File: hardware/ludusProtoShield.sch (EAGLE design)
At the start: 54 parts, among them U1 ARDUINO, U3 TB6612FNG

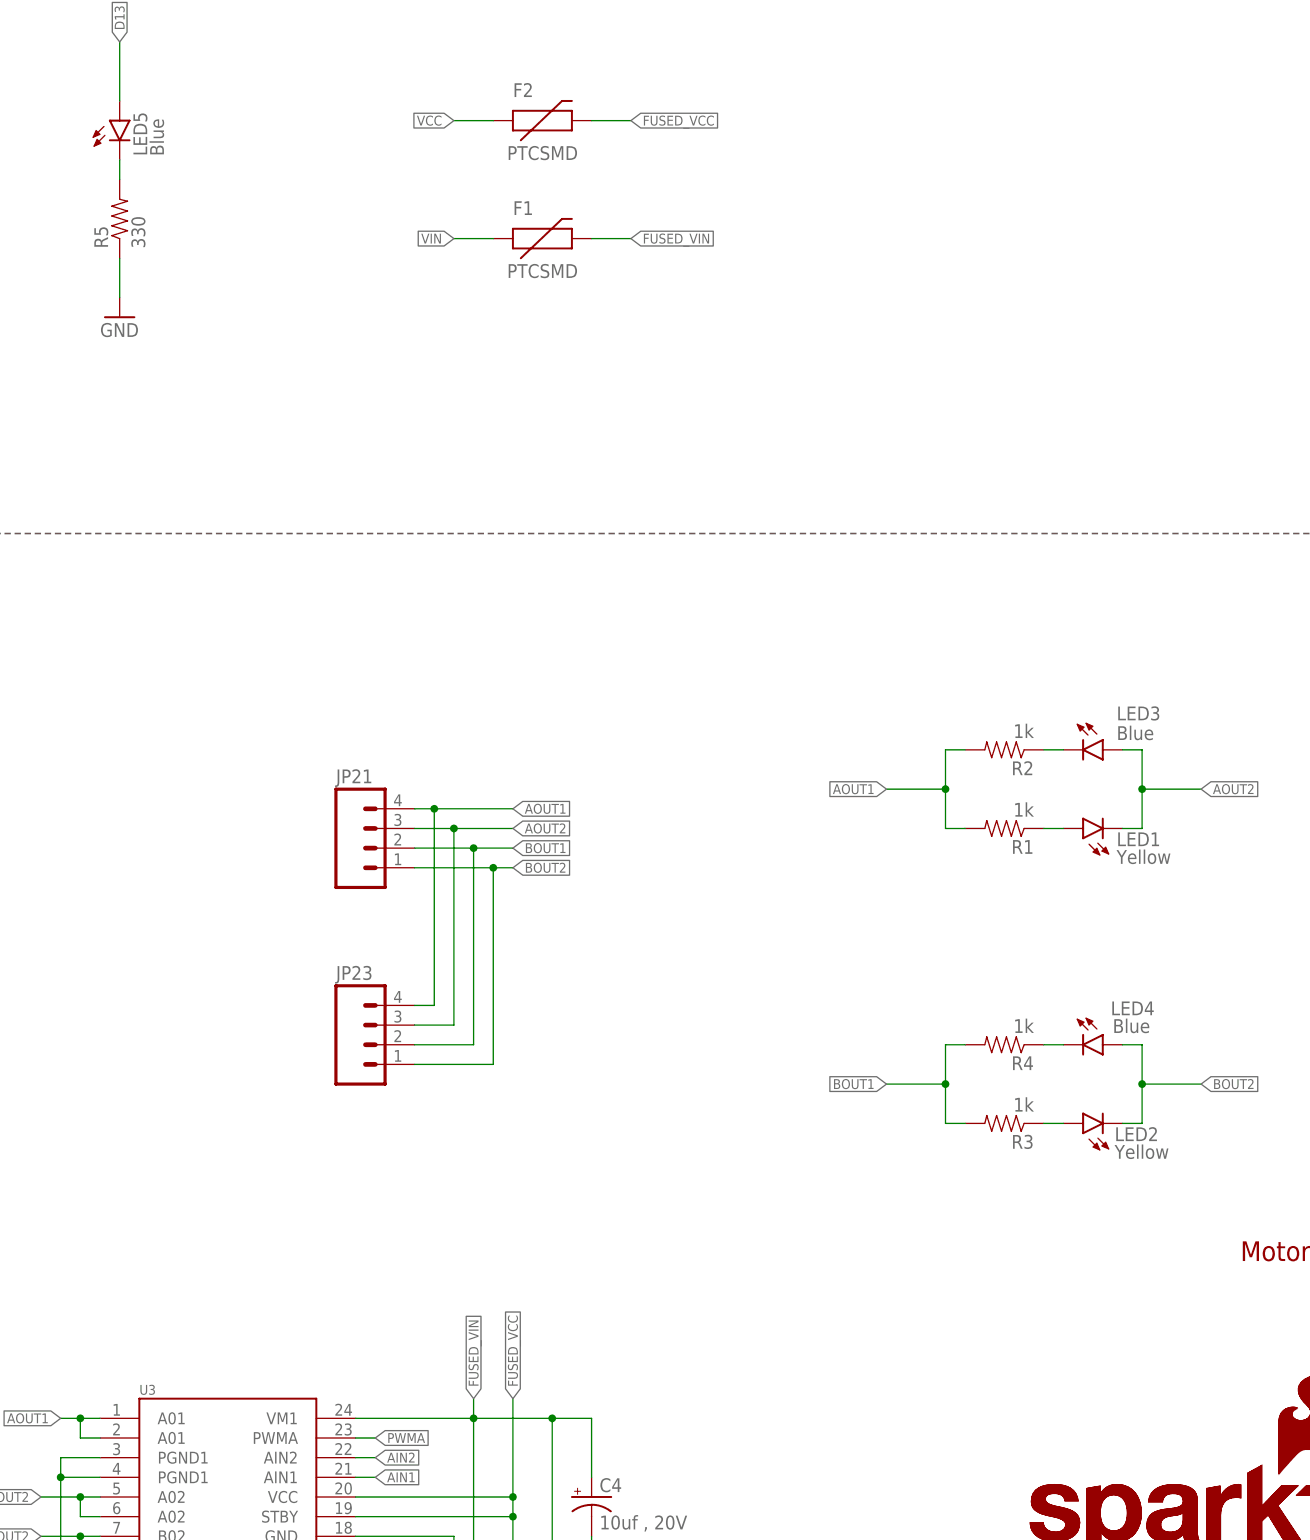
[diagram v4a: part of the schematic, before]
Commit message: Updated libraries and fixed issues from QC for Reds
Updated all of the product libraries and cleaned up extra labels in
hidden layers per issues #10-14
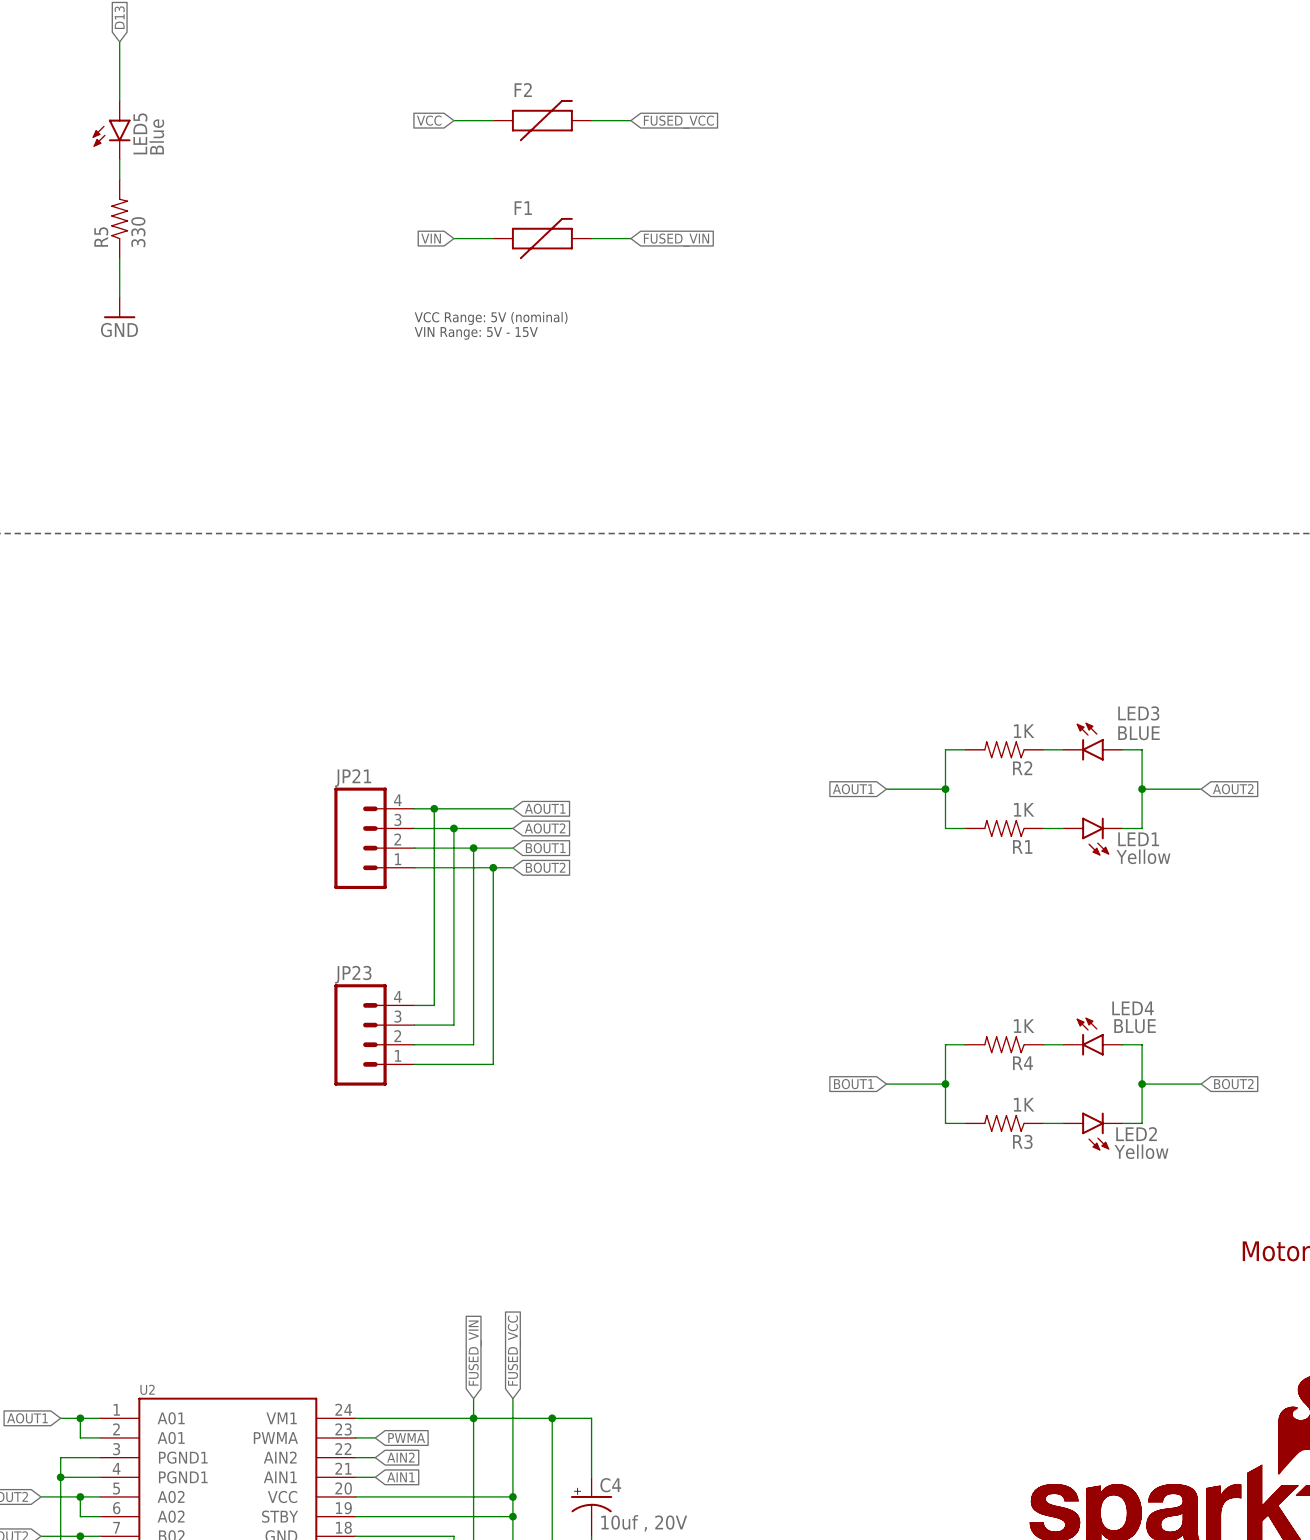
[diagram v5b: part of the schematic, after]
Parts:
- LED1, LED2: device SparkFun-LED:LED0603 -> SparkFun-LED:LED-YELLOW0603
- LED3, LED4: value Blue -> BLUE; device SparkFun-LED:LED0603 -> SparkFun-LED:LED-BLUE0603
- R1, R2, R3, R4: value 1k -> 1K; device SparkFun-Resistors:1KOHM1/10W1%(0603) -> SparkFun-Resistors:1KOHM-1/10W-1%(0603)
- renumbered U3 to U2
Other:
- note added: "VCC Range: 5V (nominal) VIN Range: 5V - 15V"

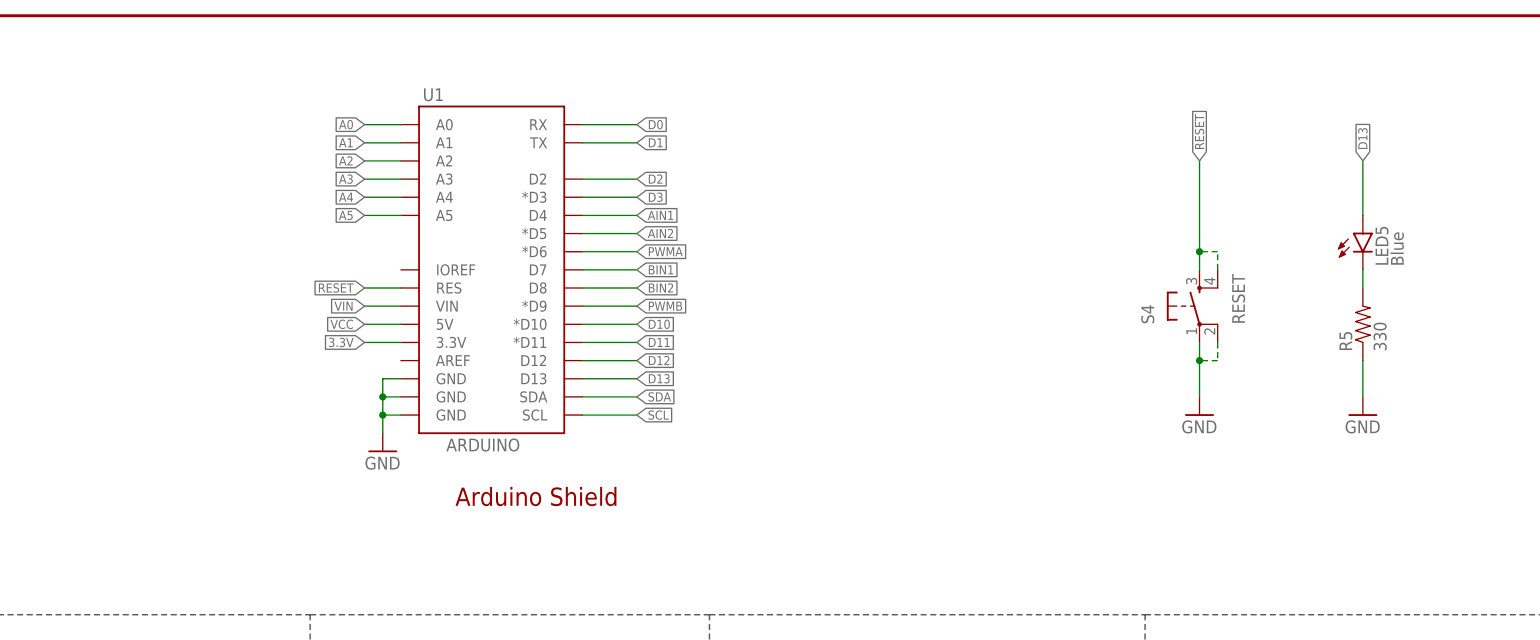
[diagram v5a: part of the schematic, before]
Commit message: Added QC testpoints to board
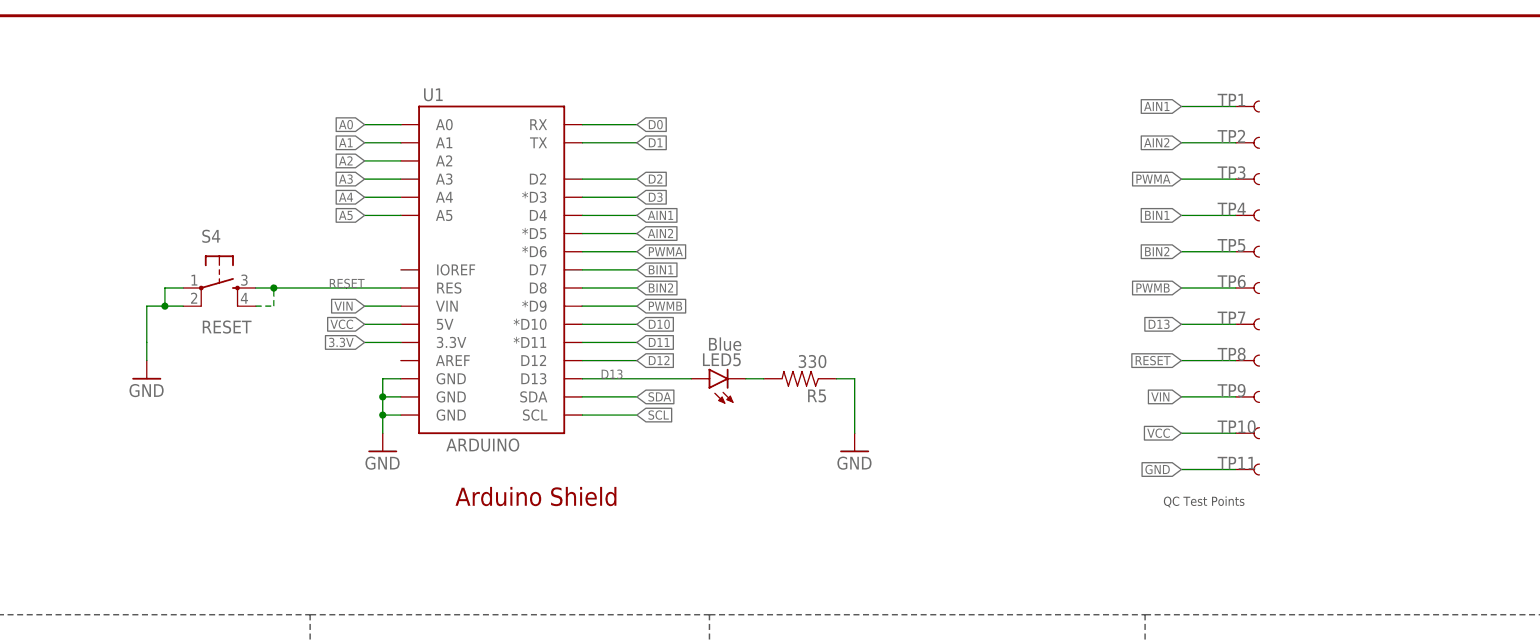
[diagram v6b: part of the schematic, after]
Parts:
- added TP1, TP10, TP11, TP2, TP3, TP4, TP5, TP6, TP7, TP8, TP9: TEST-POINT3X5, SparkFun-Passives:TEST-POINT3X5
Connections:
- net AIN1: now also TP1.1
- net AIN2: now also TP2.1
- net BIN1: now also TP4.1
- net BIN2: now also TP5.1
- net D13: now also TP7.1
- net GND: now also TP11.1
- net PWMA: now also TP3.1
- net PWMB: now also TP6.1
- net RESET: now also TP8.1
- net VCC: now also TP10.1
- net VIN: now also TP9.1
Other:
- note added: "QC Test Points"
- moved on the sheet: LED5, R5, S4
